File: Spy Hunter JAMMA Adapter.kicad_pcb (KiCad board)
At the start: 2 copper layers, 111.4 x 135.4 mm, 88 parts, among them P1 1K, P2 1K, P3 10K, P4 1K, SW2 SW_DIP_SPSTx02_Slide_9.78x7.2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, U1 74LS86, U10 NE555, U11 LM386, U12 CD4099B, U2 74LS74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

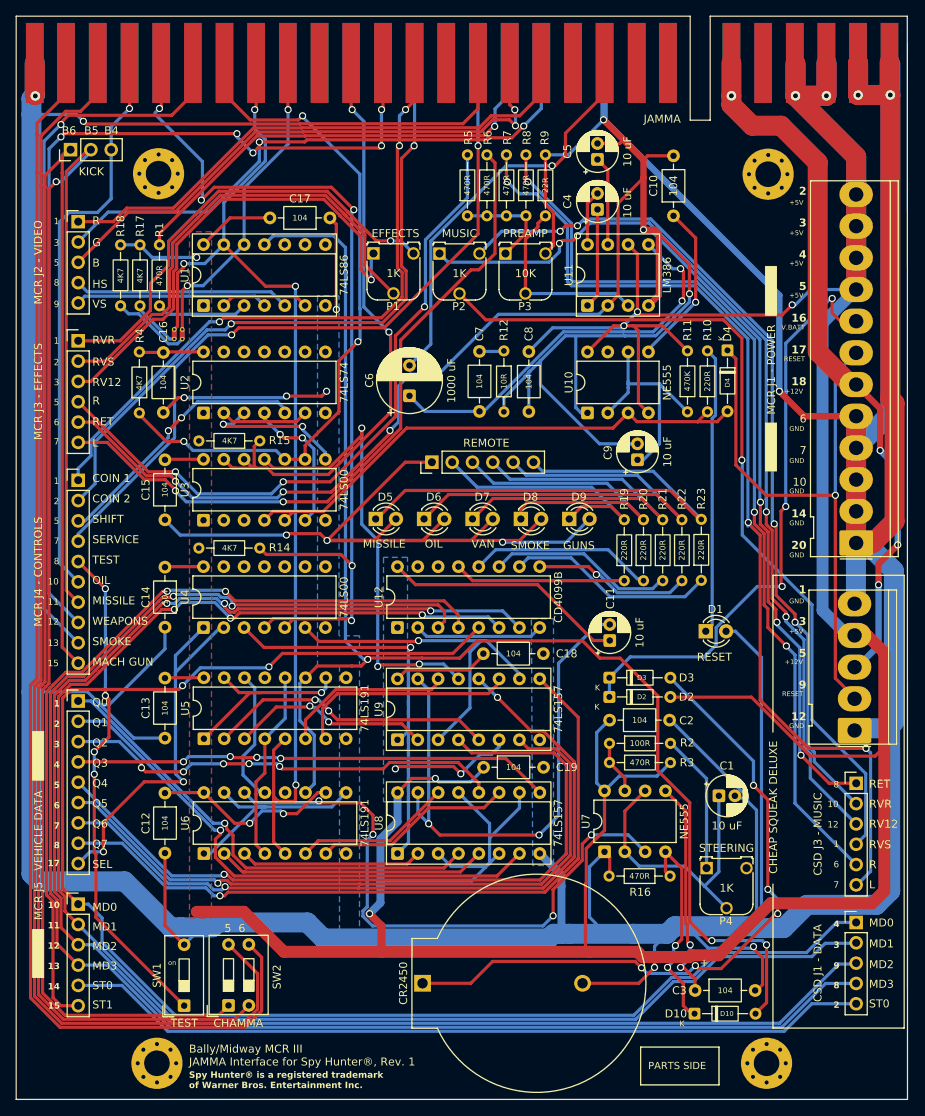
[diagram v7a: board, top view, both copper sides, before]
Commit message: move some resistor names around
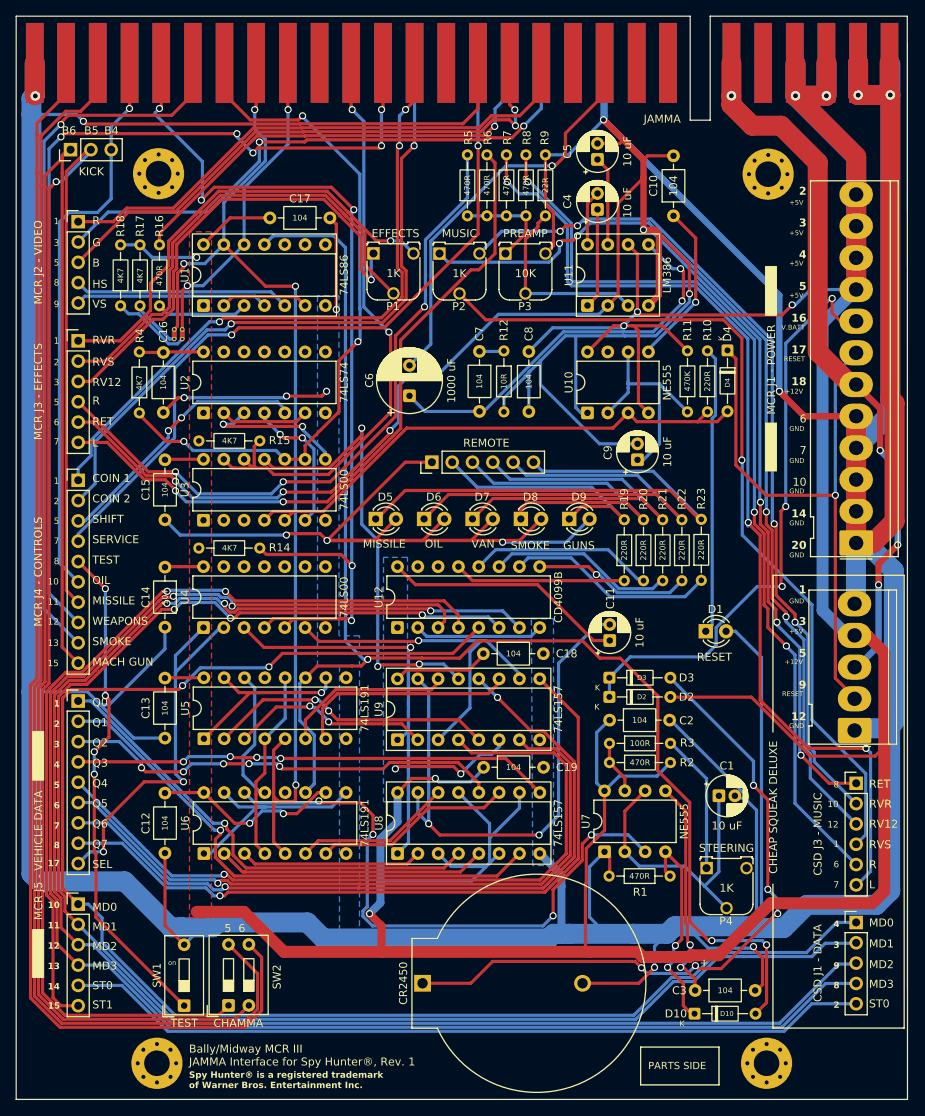
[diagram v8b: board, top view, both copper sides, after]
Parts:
- renumbered R16 to R1, R1 to R16, R3 to R2, R2 to R3
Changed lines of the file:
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@@
 		(descr "Resistor, Axial_DIN0204 series, Axial, Horizontal, pin pitch=7.62mm, 0.167W, length*diameter=3.6*1.6mm^2, http://cdn-reichelt.de/documents/datenblatt/B400/1_4W%23YAG.pdf")
 		(tags "Resistor Axial_DIN0204 series Axial Horizontal pin pitch 7.62mm 0.167W length 3.6mm diameter 1.6mm")
-		(property "Reference" "R3"
+		(property "Reference" "R2"
 			(at 9.685802 0 0)
 			(layer "F.SilkS")
@@
 		(descr "Resistor, Axial_DIN0204 series, Axial, Horizontal, pin pitch=7.62mm, 0.167W, length*diameter=3.6*1.6mm^2, http://cdn-reichelt.de/documents/datenblatt/B400/1_4W%23YAG.pdf")
 		(tags "Resistor Axial_DIN0204 series Axial Horizontal pin pitch 7.62mm 0.167W length 3.6mm diameter 1.6mm")
-		(property "Reference" "R16"
+		(property "Reference" "R1"
 			(at 3.735 -2 0)
 			(layer "F.SilkS")
@@
 		(descr "Resistor, Axial_DIN0204 series, Axial, Horizontal, pin pitch=7.62mm, 0.167W, length*diameter=3.6*1.6mm^2, http://cdn-reichelt.de/documents/datenblatt/B400/1_4W%23YAG.pdf")
 		(tags "Resistor Axial_DIN0204 series Axial Horizontal pin pitch 7.62mm 0.167W length 3.6mm diameter 1.6mm")
-		(property "Reference" "R2"
+		(property "Reference" "R3"
 			(at 9.723836 -0.074033 0)
 			(layer "F.SilkS")
@@
 		(descr "Resistor, Axial_DIN0204 series, Axial, Horizontal, pin pitch=7.62mm, 0.167W, length*diameter=3.6*1.6mm^2, http://cdn-reichelt.de/documents/datenblatt/B400/1_4W%23YAG.pdf")
 		(tags "Resistor Axial_DIN0204 series Axial Horizontal pin pitch 7.62mm 0.167W length 3.6mm diameter 1.6mm")
-		(property "Reference" "R1"
-			(at 9.497619 0 90)
+		(property "Reference" "R16"
+			(at 9.97381 0 90)
 			(layer "F.SilkS")
 			(effects
